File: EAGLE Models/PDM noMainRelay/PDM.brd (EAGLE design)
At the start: 89.7 x 75.6 mm, 20 parts

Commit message: Added new folder for pdm w/out main relay. Completed pdm w/out main relay schematic/board design. Modified pdm board layout also
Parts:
- removed U$14: VCF4-1000, relay:VCF4-1000
- added U$6: MMBD4448H-7-F, diodes-inc:SOT23-3
- moved U$10 27.3 mm to (21.4, 55.9)
- moved F5 21.3 mm to (30.5, 52.1), turned to 0 degrees
- moved U$9 15.3 mm to (45.7, 57.1)
- moved U$7 15.2 mm to (14.0, 44.5), turned to 359.9 degrees
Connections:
- removed net BAT_12V: F1.1, F1.2, U$14.NO, U$7.NO, U$9.1, U$9.2
- removed net CHARGE_SIG: U$14.COIL2, U$7.COIL1
- net 12V: now also F1.1, F1.2, U$7.NO, U$9.1, U$9.2; no longer U$14.COM
- net GND: now also U$6.3
- net KILL_SWITCH_DIODE: now also U$6.1, U$7.COIL1; no longer U$14.COIL1
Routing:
- net 12V_SHIFT_OUT: track 70.3 -> 46.6 mm
- net CHARGE_SIG: track 17.0 -> 0.00 mm
- net KILL_SWT: track 48.2 -> 56.2 mm
- net KILL_SWITCH_DIODE: track 9.60 -> 11.1 mm
- added copper zone on layer 16, net FUEL
- added copper zone on layer 1, net FUEL_12V
- removed copper zone on layer 1, net BAT_12V
- removed copper zone on layer 1, net FUEL
- removed copper zone on layer 16, net FUEL_12V

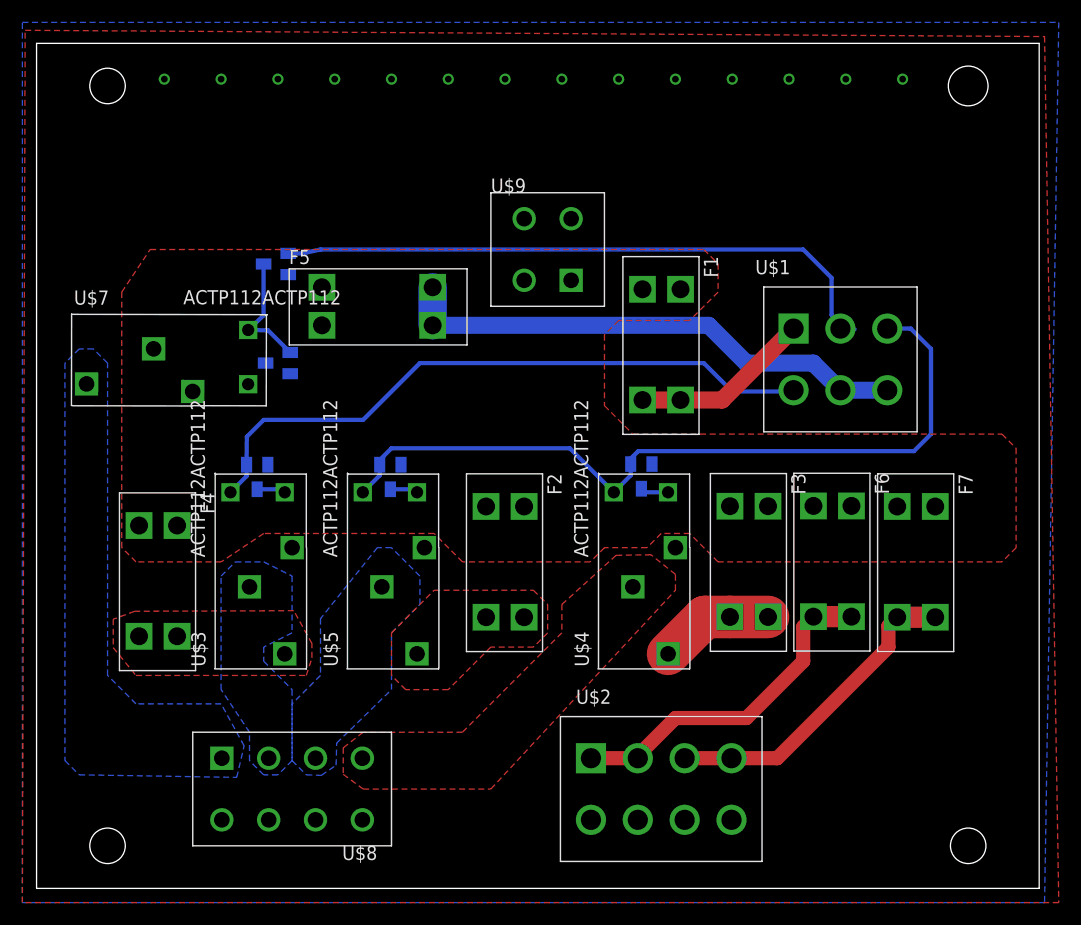
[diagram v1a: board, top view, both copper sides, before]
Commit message: Made schematic changes for PDM V2 and Ana CAN Board V2
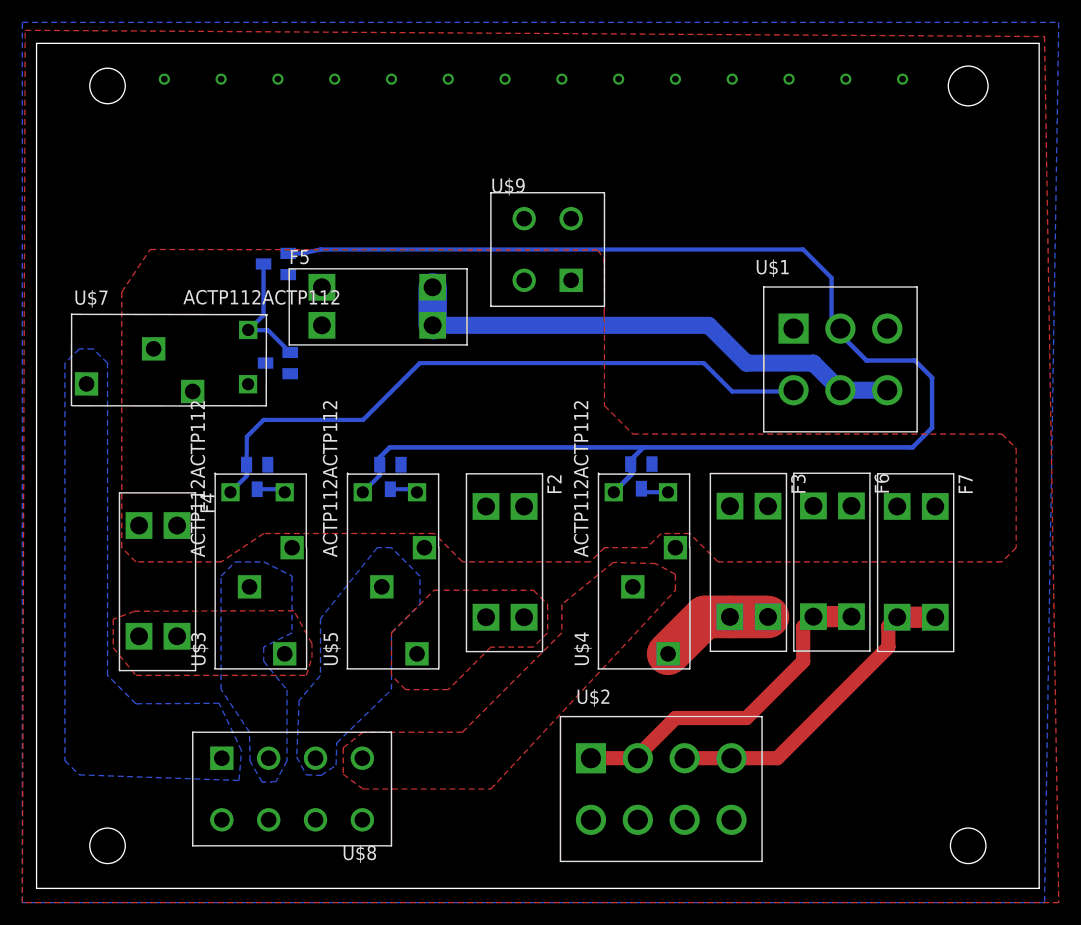
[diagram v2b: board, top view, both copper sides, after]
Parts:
- removed F1: 3568, Keystone:3568
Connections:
- removed net BAT_+12_FUSED: F1.3, F1.4, U$1.1
- removed net KILL_SWT: U$1.2, U$10.1
- new net KILL_SWT_RTRN: U$1.2, U$10.1, U$11.1, U$12.1, U$4.COIL1, U$5.COIL1
- net 12V: no longer F1.1, F1.2
- net A24: now also U$1.1; no longer U$1.3, U$11.1, U$12.1, U$4.COIL1, U$5.COIL1
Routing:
- net KILL_SWT_RTRN: track 0.00 -> 130.8 mm
- net A24: track 70.2 -> 0.00 mm
- net KILL_SWT: track 56.2 -> 0.00 mm
- net BAT_+12_FUSED: track 16.2 -> 0.00 mm
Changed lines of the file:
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@@
 </class>
 </classes>
-<designrules name="default">
+<designrules name="default *">
 <description language="de">&lt;b&gt;EAGLE Design Rules&lt;/b&gt;
 &lt;p&gt;
@@
 <param name="mdSmdStop" value="0mil"/>
 <param name="msWidth" value="10mil"/>
-<param name="msDrill" value="24mil"/>
+<param name="msDrill" value="20mil"/>
 <param name="msMicroVia" value="9.99mm"/>
 <param name="msBlindViaRatio" value="0.5"/>
@@
 <element name="U$12" library="diodes-inc" package="SOT23-3" value="MMBD4448H-7-F" x="31.6484" y="36.8046" rot="MR180"/>
 <element name="U$13" library="diodes-inc" package="SOT23-3" value="MMBD4448H-7-F" x="19.7358" y="36.8046" rot="MR180"/>
-<element name="F1" library="Keystone" package="3568" value="3568" x="55.9054" y="48.641" rot="R270"/>
 <element name="F7" library="Keystone" package="3568" value="3568" x="78.6892" y="29.21" rot="R270"/>
 <element name="U$6" library="diodes-inc" package="SOT23-3" value="MMBD4448H-7-F" x="21.59" y="46.99" rot="MR270"/>
@@
 </polygon>
 </signal>
-<signal name="A24">
-<contactref element="U$4" pad="COIL1"/>
-<contactref element="U$5" pad="COIL1"/>
-<contactref element="U$1" pad="3"/>
-<contactref element="U$11" pad="1"/>
-<contactref element="U$12" pad="1"/>
-<wire x1="76.0984" y1="50.0761" x2="78.1939" y2="50.0761" width="0.381" layer="16"/>
-<wire x1="78.1939" y1="50.0761" x2="80.01" y2="48.26" width="0.381" layer="16"/>
-<wire x1="51.6382" y1="35.433" x2="53.152" y2="36.9468" width="0.381" layer="16"/>
-<wire x1="53.152" y1="36.9468" x2="53.152" y2="37.9554" width="0.381" layer="16"/>
-<wire x1="53.152" y1="37.9554" x2="53.152" y2="38.4454" width="0.381" layer="16"/>
-<wire x1="53.152" y1="38.4454" x2="53.8226" y2="39.116" width="0.381" layer="16"/>
-<wire x1="53.8226" y1="39.116" x2="78.486" y2="39.116" width="0.381" layer="16"/>
-<wire x1="78.486" y1="39.116" x2="80.01" y2="40.64" width="0.381" layer="16"/>
-<wire x1="80.01" y1="40.64" x2="80.01" y2="48.26" width="0.381" layer="16"/>
-<wire x1="30.6984" y1="37.9046" x2="30.6984" y2="36.9468" width="0.381" layer="16"/>
-<wire x1="30.6984" y1="36.9468" x2="29.1846" y2="35.433" width="0.381" layer="16"/>
-<wire x1="30.6984" y1="37.9046" x2="30.6984" y2="38.3184" width="0.381" layer="16"/>
-<wire x1="30.6984" y1="38.3184" x2="31.75" y2="39.37" width="0.381" layer="16"/>
-<wire x1="31.75" y1="39.37" x2="47.7012" y2="39.37" width="0.381" layer="16"/>
-<wire x1="47.7012" y1="39.37" x2="51.6382" y2="35.433" width="0.381" layer="16"/>
-</signal>
 <signal name="FAN">
 <contactref element="U$3" pad="NO"/>
@@
 <vertex x="20.32" y="21.59"/>
 <vertex x="20.32" y="20.32"/>
-<vertex x="22.86" y="17.78"/>
-<vertex x="22.86" y="11.43"/>
-<vertex x="21.59" y="10.16"/>
-<vertex x="20.32" y="10.16"/>
-<vertex x="19.05" y="11.43"/>
+<vertex x="22.4028" y="17.7546"/>
+<vertex x="22.4028" y="11.4046"/>
+<vertex x="21.4122" y="9.5504"/>
+<vertex x="20.193" y="9.4996"/>
+<vertex x="19.1008" y="11.3792"/>
 <vertex x="19.05" y="13.97"/>
 <vertex x="16.51" y="17.78"/>
@@
 <vertex x="57.15" y="26.67"/>
 <vertex x="57.15" y="28.0924"/>
-<vertex x="54.9656" y="29.845"/>
-<vertex x="51.8414" y="29.7942"/>
+<vertex x="55.372" y="29.0576"/>
+<vertex x="51.5874" y="29.1592"/>
 <vertex x="46.99" y="25.4"/>
 <vertex x="46.99" y="22.86"/>
@@
 <contactref element="U$8" pad="3"/>
 <polygon width="0.381" layer="16">
-<vertex x="22.86" y="11.43"/>
+<vertex x="23.2664" y="11.7602"/>
 <vertex x="24.13" y="10.16"/>
 <vertex x="25.4762" y="10.1092"/>
@@
 <vertex x="25.4" y="24.13"/>
 <vertex x="25.4" y="19.05"/>
-<vertex x="22.86" y="16.51"/>
+<vertex x="23.495" y="16.8148"/>
 </polygon>
 </signal>
@@
 <vertex x="2.54" y="11.43"/>
 <vertex x="3.81" y="10.16"/>
-<vertex x="17.907" y="9.9314"/>
-<vertex x="18.5674" y="12.7508"/>
-<vertex x="16.51" y="16.51"/>
+<vertex x="18.1102" y="9.652"/>
+<vertex x="18.3388" y="12.319"/>
+<vertex x="16.3322" y="16.5608"/>
 <vertex x="8.89" y="16.51"/>
 <vertex x="6.35" y="19.05"/>
@@
 <vertex x="5.08" y="48.26"/>
 </polygon>
-</signal>
-<signal name="KILL_SWT">
-<contactref element="U$1" pad="2"/>
-<contactref element="U$10" pad="1"/>
-<wire x1="71.9074" y1="50.0761" x2="71.9074" y2="50.0126" width="0.381" layer="16"/>
-<wire x1="71.9074" y1="50.0126" x2="72.39" y2="50.0126" width="0.381" layer="16"/>
-<wire x1="72.39" y1="50.0126" x2="73.1774" y2="50.0126" width="0.381" layer="16"/>
-<wire x1="22.5122" y1="56.8046" x2="23.7846" y2="56.8046" width="0.381" layer="16"/>
-<wire x1="23.7846" y1="56.8046" x2="25.4" y2="57.15" width="0.381" layer="16"/>
-<wire x1="25.4" y1="57.15" x2="68.58" y2="57.15" width="0.381" layer="16"/>
-<wire x1="68.58" y1="57.15" x2="71.12" y2="54.61" width="0.381" layer="16"/>
-<wire x1="71.12" y1="54.61" x2="71.12" y2="51.2826" width="0.381" layer="16"/>
-<wire x1="71.12" y1="51.2826" x2="72.39" y2="50.0126" width="0.381" layer="16"/>
 </signal>
 <signal name="12V_SHIFT_OUT">
@@
 <wire x1="21.928" y1="35.7046" x2="22.1996" y2="35.433" width="0.381" layer="16"/>
 <contactref element="U$7" pad="NO"/>
-<contactref element="F1" pad="1"/>
-<contactref element="F1" pad="2"/>
 <contactref element="U$9" pad="2"/>
 <contactref element="U$9" pad="1"/>
@@
 <vertex x="7.62" y="53.34"/>
 <vertex x="10.16" y="57.15"/>
-<vertex x="59.69" y="57.15"/>
-<vertex x="60.96" y="55.88"/>
-<vertex x="60.96" y="53.34"/>
-<vertex x="58.42" y="50.8"/>
-<vertex x="52.07" y="50.8"/>
+<vertex x="50.1904" y="57.0992"/>
+<vertex x="50.7746" y="56.3372"/>
+<vertex x="50.8" y="51.7652"/>
+<vertex x="50.7746" y="51.5112"/>
+<vertex x="50.7746" y="51.1302"/>
 <vertex x="50.8" y="49.53"/>
 <vertex x="50.8" y="43.18"/>
@@
 </polygon>
 </signal>
-<signal name="BAT_+12_FUSED">
-<contactref element="U$1" pad="1"/>
-<contactref element="F1" pad="3"/>
-<contactref element="F1" pad="4"/>
-<wire x1="54.2036" y1="43.688" x2="57.6072" y2="43.688" width="1.524" layer="1"/>
-<wire x1="57.6072" y1="43.688" x2="61.3283" y2="43.688" width="1.524" layer="1"/>
-<wire x1="61.3283" y1="43.688" x2="67.7164" y2="50.0761" width="1.524" layer="1"/>
-</signal>
 <signal name="12V_FUSED_ECU">
 <contactref element="F7" pad="3"/>
@@
 <wire x1="20.711634375" y1="49.918365625" x2="22.69" y2="47.94" width="0.381" layer="16"/>
 </signal>
+<signal name="A24">
+<contactref element="U$1" pad="1"/>
+</signal>
+<signal name="KILL_SWT_RTRN">
+<contactref element="U$1" pad="2"/>
+<contactref element="U$4" pad="COIL1"/>
+<contactref element="U$5" pad="COIL1"/>
+<contactref element="U$11" pad="1"/>
+<contactref element="U$12" pad="1"/>
+<wire x1="30.6984" y1="37.9046" x2="30.6984" y2="36.9468" width="0.381" layer="16"/>
+<wire x1="30.6984" y1="36.9468" x2="29.1846" y2="35.433" width="0.381" layer="16"/>
+<wire x1="30.6984" y1="37.9046" x2="30.6984" y2="38.3184" width="0.381" layer="16"/>
+<contactref element="U$10" pad="1"/>
+<wire x1="22.5122" y1="56.8046" x2="23.7846" y2="56.8046" width="0.381" layer="16"/>
+<wire x1="23.7846" y1="56.8046" x2="25.4" y2="57.15" width="0.381" layer="16"/>
+<wire x1="25.4" y1="57.15" x2="68.58" y2="57.15" width="0.381" layer="16"/>
+<wire x1="68.58" y1="57.15" x2="71.12" y2="54.61" width="0.381" layer="16"/>
+<wire x1="71.12" y1="54.61" x2="71.12" y2="51.2826" width="0.381" layer="16"/>
+<wire x1="71.12" y1="51.2826" x2="71.12" y2="50.8635" width="0.4064" layer="16"/>
+<wire x1="30.6984" y1="38.3184" x2="30.6984" y2="38.547" width="0.4064" layer="16"/>
+<wire x1="30.6984" y1="38.547" x2="31.5976" y2="39.4462" width="0.4064" layer="16"/>
+<wire x1="31.5976" y1="39.4462" x2="54.2798" y2="39.4462" width="0.4064" layer="16"/>
+<wire x1="54.2798" y1="39.4462" x2="78.359" y2="39.4462" width="0.4064" layer="16"/>
+<wire x1="78.359" y1="39.4462" x2="80.1116" y2="41.1988" width="0.4064" layer="16"/>
+<wire x1="80.1116" y1="41.1988" x2="80.1116" y2="45.6692" width="0.4064" layer="16"/>
+<wire x1="80.1116" y1="45.6692" x2="78.5622" y2="47.2186" width="0.4064" layer="16"/>
+<wire x1="78.5622" y1="47.2186" x2="74.2442" y2="47.2186" width="0.4064" layer="16"/>
+<wire x1="74.2442" y1="47.2186" x2="71.9074" y2="49.5554" width="0.4064" layer="16"/>
+<wire x1="71.9074" y1="49.5554" x2="71.9074" y2="50.0761" width="0.4064" layer="16"/>
+<wire x1="51.6382" y1="35.433" x2="53.152" y2="36.9468" width="0.4064" layer="16"/>
+<wire x1="53.152" y1="36.9468" x2="53.152" y2="37.9554" width="0.4064" layer="16"/>
+<wire x1="51.6382" y1="35.433" x2="53.34" y2="37.1348" width="0.4064" layer="16"/>
+<wire x1="53.34" y1="37.1348" x2="53.34" y2="38.5064" width="0.4064" layer="16"/>
+<wire x1="53.34" y1="38.5064" x2="54.2798" y2="39.4462" width="0.4064" layer="16"/>
+<wire x1="71.9074" y1="50.0761" x2="71.12" y2="50.8635" width="0" layer="19" extent="16-16"/>
+</signal>
 </signals>

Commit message: Added silk screens
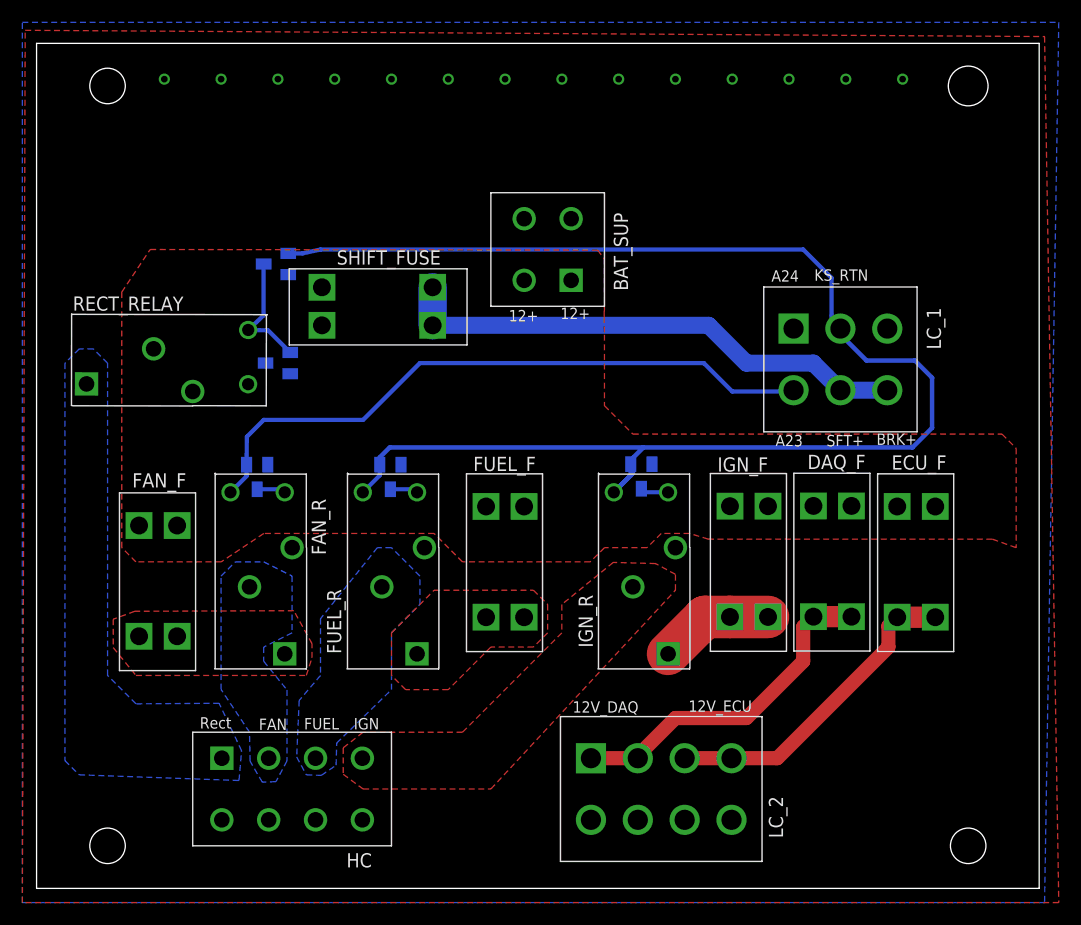
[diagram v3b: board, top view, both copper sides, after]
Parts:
- renumbered F2 to FUEL_F, F3 to IGN_F, F4 to FAN_F, F5 to SHIFT_FUSE, F6 to DAQ_F, F7 to ECU_F, U$1 to LC_1, U$10 to K_SWT_D, U$11 to IGN_D, U$12 to FUEL_D, U$13 to FAN_D, U$2 to LC_2, U$3 to FAN_R, U$4 to IGN_R, U$5 to FUEL_R, U$6 to CC_D, U$7 to RECT_RELAY, U$8 to HC, U$9 to BAT_SUP
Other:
- board text added: "12+"
- board text added: "12V_DAQ"
- board text added: "12V_ECU"
- board text added: "A23"
- board text added: "A24"
- board text added: "BRK+"
- board text added: "FAN"
- board text added: "FUEL"
- board text added: "IGN"
- board text added: "KS_RTN"
- board text added: "LC_2"
- board text added: "Rect"
- board text added: "SFT+"

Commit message: Updated Analog CAN board protection as per thomas's reccomendation
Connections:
- removed net A24: LC_1.1
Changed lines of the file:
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@@
 <wire x1="20.711634375" y1="49.918365625" x2="22.69" y2="47.94" width="0.381" layer="16"/>
-</signal>
-<signal name="A24">
-<contactref element="LC_1" pad="1"/>
 </signal>
 <signal name="KILL_SWT_RTRN">
